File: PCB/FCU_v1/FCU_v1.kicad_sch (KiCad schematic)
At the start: 20 parts, among them J1 Conn_01x04_Pin, J10 Conn_01x04_Pin, J5 Conn_01x04_Pin, J6 Conn_01x04_Pin, J7 Conn_01x04_Pin, J8 Conn_01x04_Pin, J9 Conn_01x04_Pin, U1 TPS62132

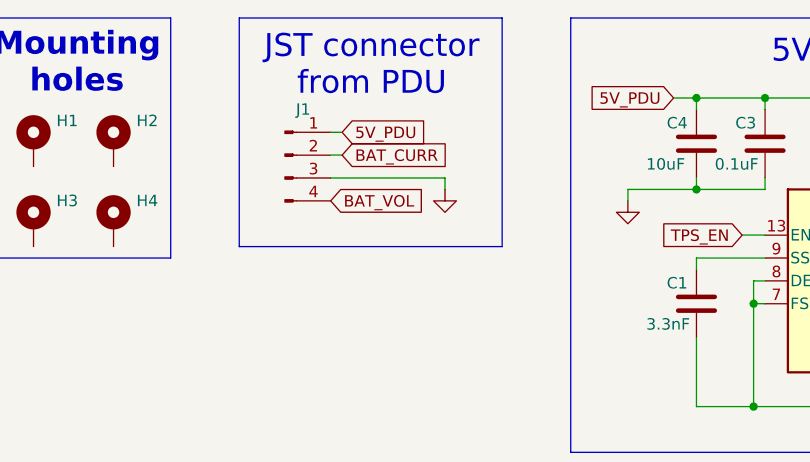
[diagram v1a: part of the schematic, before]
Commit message: Update PCB footprints, positions and backups
Remove old FCU_v1 backup zips and add new timestamped backups. Apply extensive edits to PCB/FCU_v1.kicad_pcb: reposition and rotate multiple footprints, fix pad orientations, update silkscreen/fab/crtyd outlines and UUIDs, change some net mappings and sheet/path references, and replace a resistor footprint with a SOT-23-6 ESD device (USBLC6) including updated properties and datasheet. Update related project/schematic files (FCU_v1.kicad_prl, FCU_v1.kicad_sch, PERIPHERALS.kicad_sch) to reflect these changes.
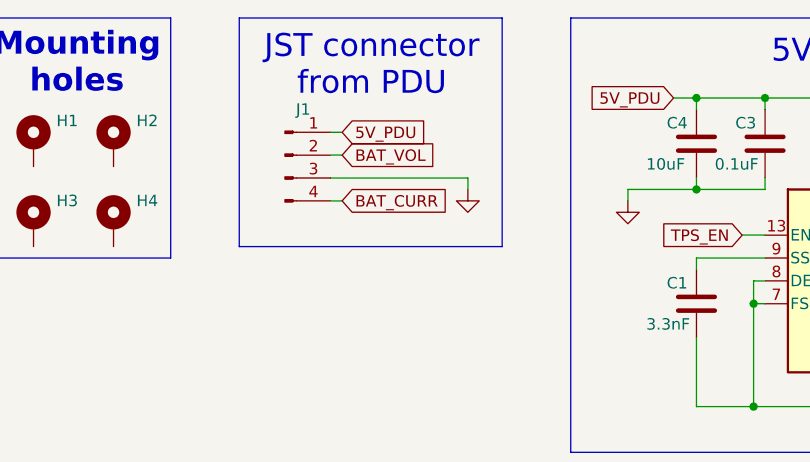
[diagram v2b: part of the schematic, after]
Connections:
- net BAT_CURR: now also J1.4 (Pin_4); no longer J1.2 (Pin_2)
- net BAT_VOL: now also J1.2 (Pin_2); no longer J1.4 (Pin_4)
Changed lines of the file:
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@@
 	(wire
 		(pts
-			(xy 69.85 36.83) (xy 69.85 38.1)
+			(xy 72.39 36.83) (xy 72.39 38.1)
 		)
 		(stroke
@@
 	(wire
 		(pts
+			(xy 57.15 39.37) (xy 58.42 39.37)
+		)
+		(stroke
+			(width 0)
+			(type default)
+		)
+	)
+	(wire
+		(pts
 			(xy 104.14 48.26) (xy 104.14 50.8)
 		)
@@
 	(wire
 		(pts
-			(xy 57.15 36.83) (xy 69.85 36.83)
+			(xy 57.15 36.83) (xy 72.39 36.83)
 		)
 		(stroke
@@
 		)
 	)
-	(global_label "BAT_CURR"
-		(shape input)
-		(at 58.42 34.29 0)
-		(fields_autoplaced yes)
-		(effects
-			(font
-				(size 1.27 1.27)
-			)
-			(justify left)
-		)
-		(property "Intersheetrefs" "${INTERSHEET_REFS}"
-			(at 70.8395 34.29 0)
-			(effects
-				(font
-					(size 1.27 1.27)
-				)
-				(justify left)
-				(hide yes)
-			)
-		)
-	)
 	(global_label "3V3"
 		(shape input)
@@
 		)
 	)
-	(global_label "3V3"
+	(global_label "BAT_VOL"
 		(shape input)
-		(at 33.02 87.63 0)
+		(at 58.42 34.29 0)
 		(fields_autoplaced yes)
 		(effects
@@
 		)
 		(property "Intersheetrefs" "${INTERSHEET_REFS}"
-			(at 39.5128 87.63 0)
+			(at 69.1462 34.29 0)
 			(effects
 				(font
@@
 		)
 	)
-	(global_label "CAN_H"
+	(global_label "3V3"
 		(shape input)
-		(at 33.02 111.76 0)
+		(at 33.02 87.63 0)
 		(fields_autoplaced yes)
 		(effects
@@
 		)
 		(property "Intersheetrefs" "${INTERSHEET_REFS}"
-			(at 41.9924 111.76 0)
+			(at 39.5128 87.63 0)
 			(effects
 				(font
@@
 		)
 	)
-	(global_label "3V3"
+	(global_label "CAN_H"
 		(shape input)
-		(at 33.02 104.14 0)
+		(at 33.02 111.76 0)
 		(fields_autoplaced yes)
 		(effects
@@
 		)
 		(property "Intersheetrefs" "${INTERSHEET_REFS}"
-			(at 39.5128 104.14 0)
+			(at 41.9924 111.76 0)
 			(effects
 				(font
@@
 		)
 	)
-	(global_label "BAT_VOL"
+	(global_label "3V3"
 		(shape input)
-		(at 57.15 39.37 0)
+		(at 33.02 104.14 0)
 		(fields_autoplaced yes)
 		(effects
@@
 		)
 		(property "Intersheetrefs" "${INTERSHEET_REFS}"
-			(at 67.8762 39.37 0)
+			(at 39.5128 104.14 0)
 			(effects
 				(font
@@
 		)
 	)
+	(global_label "BAT_CURR"
+		(shape input)
+		(at 58.42 39.37 0)
+		(fields_autoplaced yes)
+		(effects
+			(font
+				(size 1.27 1.27)
+			)
+			(justify left)
+		)
+		(property "Intersheetrefs" "${INTERSHEET_REFS}"
+			(at 70.8395 39.37 0)
+			(effects
+				(font
+					(size 1.27 1.27)
+				)
+				(justify left)
+				(hide yes)
+			)
+		)
+	)
 	(global_label "CAN_L"
 		(shape input)
@@
 	(symbol
 		(lib_id "power:GND")
-		(at 69.85 38.1 0)
+		(at 72.39 38.1 0)
 		(unit 1)
 		(exclude_from_sim no)
@@
 		(fields_autoplaced yes)
 		(property "Reference" "#PWR016"
-			(at 69.85 44.45 0)
+			(at 72.39 44.45 0)
 			(effects
 				(font
@@
 		)
 		(property "Value" "GND"
-			(at 69.85 43.18 0)
+			(at 72.39 43.18 0)
 			(effects
 				(font
@@
 		)
 		(property "Footprint" ""
-			(at 69.85 38.1 0)
+			(at 72.39 38.1 0)
 			(effects
 				(font
@@
 		)
 		(property "Datasheet" ""
-			(at 69.85 38.1 0)
+			(at 72.39 38.1 0)
 			(effects
 				(font
@@
 		)
 		(property "Description" "Power symbol creates a global label with name \"GND\" , ground"
-			(at 69.85 38.1 0)
+			(at 72.39 38.1 0)
 			(effects
 				(font

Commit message: Schematic update
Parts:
- removed C3: 0.1uF, Capacitor_SMD:C_0805_2012Metric, symbol Device:C
- removed L2: 2.2uH, Inductor_SMD:L_Coilcraft_XxL4020, symbol Device:L
- removed U1: TPS62132, Package_DFN_QFN:VQFN-16-1EP_3x3mm_P0.5mm_EP1.68x1.68mm_ThermalVias, symbol Regulator_Switching:TPS62132
- added C17: 22u, Capacitor_SMD:C_0805_2012Metric, symbol Device:C
- added C20: 100n, Capacitor_SMD:C_0805_2012Metric, symbol Device:C
- added D3: BAT54CWFILMY, Package_TO_SOT_SMD:SOT-323_SC-70, symbol Diode:BAT54CW
- added D6: SMF54A, Diode_SMD:D_SMF, symbol Diode:SMF54A
- added FB2: 120R at 100 MHz, Inductor_SMD:L_0805_2012Metric, symbol Device:FerriteBead
- added J11: USB_C_Receptacle_USB2.0_16P, Connector_USB:USB_C_Receptacle_GCT_USB4105-xx-A_16P_TopMnt_Horizontal, symbol Connector:USB_C_Receptacle_USB2.0_16P
- added L1: 744042001, SamacSys_Parts:WE-TPC_4818_482892, symbol SamacSys_Parts:744042001
- added R35, R36: 5k1, Resistor_SMD:R_0603_1608Metric, symbol Device:R
- added R37: 100k, Resistor_SMD:R_0603_1608Metric, symbol Device:R
- added R4: 33k, Resistor_SMD:R_0603_1608Metric, symbol Device:R
- added R5: 82k, Resistor_SMD:R_0603_1608Metric, symbol Device:R
- added U1: TPS62A02APDDCR, Package_TO_SOT_SMD:SOT-23-6, symbol Regulator_Switching:TPS62A02APDDC
- added U8: USBLC6-2SC6, Package_TO_SOT_SMD:SOT-23-6, symbol Power_Protection:USBLC6-2SC6
- C1: value 3.3nF -> 22u/10V
- C2: value 22uF -> 100n/10V
- C4: value 10uF -> 10u/10V
- R1: value 100k -> 2k
- R2: value 4.7k -> 450k
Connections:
- net GND: now also C17.2, C20.2, D6.2 (A2), J11.A1 (GND), J11.A12 (GND), J11.B1 (GND), J11.B12 (GND), J11.S1 (SHIELD), R35.1, R36.1, R37.2, R5.1, U1.2 (GND), U1.5 (PG), U8.2 (GND)
- net at D1.2 (A): now also R1.2; no longer R2.2
- net +3.3V: now reaches C1.1
- net +3.3V: now also R1.1, R2.1, L1.2
- net 3V3 renamed +5V
- net +5V: now also J1.1 (Pin_1), D3.2; no longer C2.1, R1.1, R2.1
- net 5V_PDU renamed +5V_FCU
- net +5V_FCU: now also C2.1, D3.3, U1.1 (EN), U1.4 (VIN); no longer J1.1 (Pin_1)
- new net: J11.A5 (CC1), R36.2
- new net: L1.1, U1.3 (SW)
- new net: R2.2, R37.1, U1.6 (FB)
- new net: J11.B5 (CC2), R35.2
- new net +VBUS: C17.1, C20.1, D3.1, FB2.2, R4.2
- new net D+: J11.A6 (D+), J11.B6 (D+), U8.6 (I/O1)
- new net D-: J11.A7 (D-), J11.B7 (D-), U8.4 (I/O2)
- new net USB_D+: U8.1 (I/O1)
- new net USB_D-: U8.3 (I/O2)
- new net USB_VBUS: D6.1 (A1), FB2.1, J11.A4 (VBUS), J11.A9 (VBUS), J11.B4 (VBUS), J11.B9 (VBUS), U8.5 (VBUS)
- new net VBUS_SENS: R4.1, R5.2
- no-connect marks 0 -> 2
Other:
- sheet PERIPHERALS renamed OLD_UNUSED
- added sheet ESP (ESP.kicad_sch)
- added sheet IMU (IMU.kicad_sch)
- sheet OLD_UNUSED: file PERIPHERALS.kicad_sch -> OLD_UNUSED.kicad_sch
- note added: "BAT54CWFILMY"
- note added: "PDB/USB 5V source"
- note added: "To STM for measurements"
- note added: "USB"
- note added: "Wurth 744042001"
- moved on the sheet: C4, D1, H1, H2, H3, H4, J1, J10, J5, J6, J7, J8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

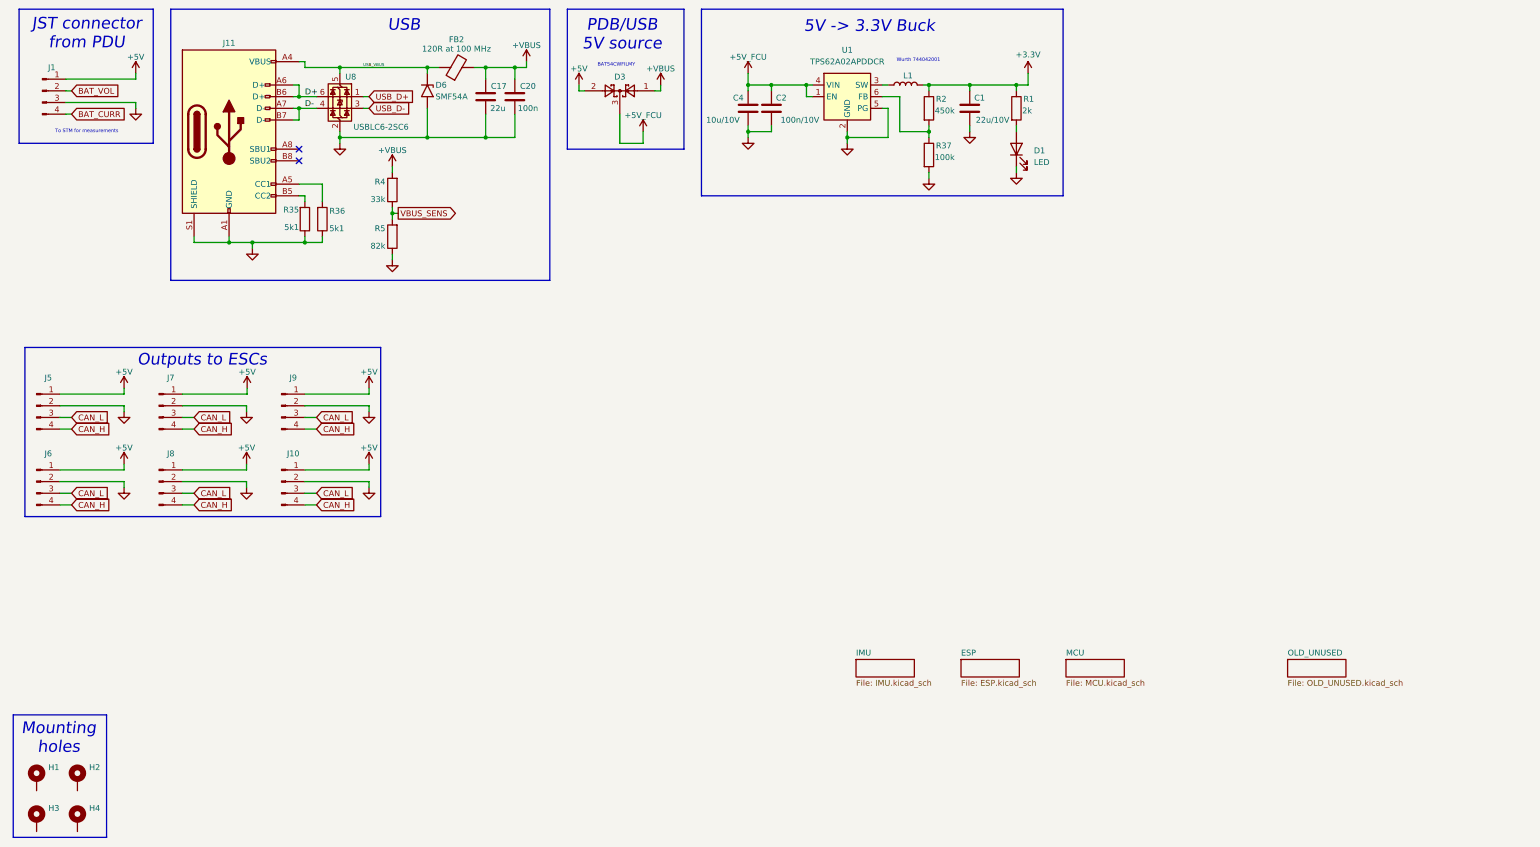
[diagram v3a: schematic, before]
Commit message: Components change and layout update
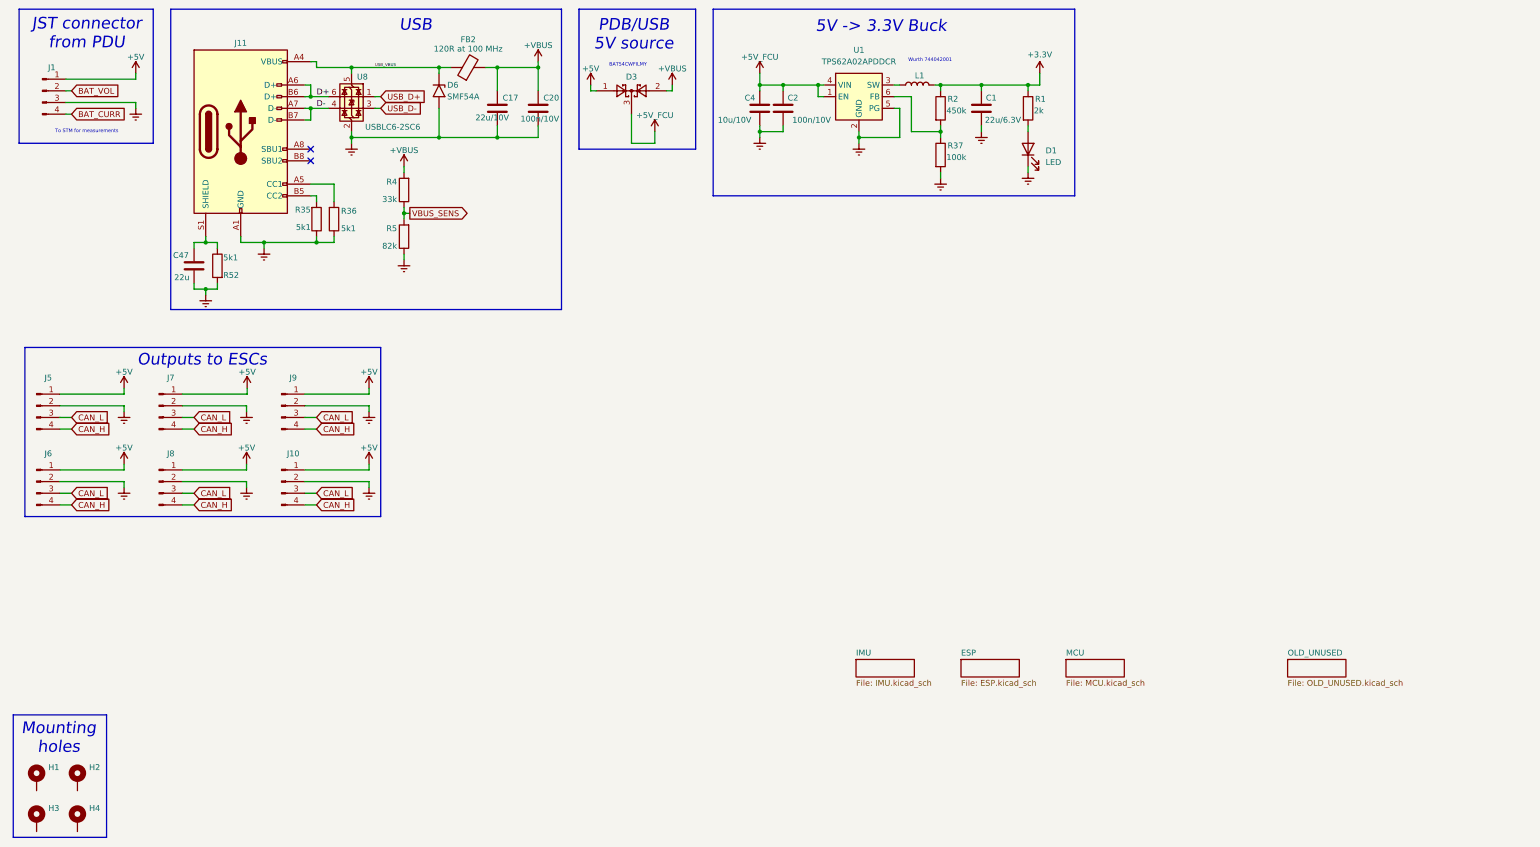
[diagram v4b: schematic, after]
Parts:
- added C47: 22u, Capacitor_SMD:C_0805_2012Metric, symbol Device:C
- added R52: 5k1, Resistor_SMD:R_0603_1608Metric, symbol Device:R
- C1: value 22u/10V -> 22u/6.3V
- C17: value 22u -> 22u/10V
- C2: footprint Capacitor_SMD:C_0805_2012Metric -> Capacitor_SMD:C_0603_1608Metric
- C20: value 100n -> 100n/10V
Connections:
- net +5V: now also D3.1; no longer D3.2
- net +VBUS: now also D3.2; no longer D3.1
- net GND: now also C47.2, R52.2; no longer J11.S1 (SHIELD)
- new net: C47.1, J11.S1 (SHIELD), R52.1
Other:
- moved on the sheet: C1, C17, C2, C20, C4, D1, D3, D6, FB2, J11, L1, R1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

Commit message: Layout update
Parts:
- removed L1: 744042001, SamacSys_Parts:WE-TPC_4818_482892, symbol SamacSys_Parts:744042001
- removed U8: USBLC6-2SC6, Package_TO_SOT_SMD:SOT-23-6, symbol Power_Protection:USBLC6-2SC6
- added L4: 744042001, SamacSys_Parts:WE-TPC_4818_482892, symbol SamacSys_Parts:744042001
- added U7: USBLC6-2SC6, Package_TO_SOT_SMD:SOT-23-6, symbol Power_Protection:USBLC6-2SC6
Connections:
- net +3.3V: now also L4.2
- net D+: now also U7.6 (I/O1)
- net D-: now also U7.4 (I/O2)
- net GND: now also U7.2 (GND)
- net USB_D+: now also U7.1 (I/O1)
- net USB_D-: now also U7.3 (I/O2)
- net USB_VBUS: now also U7.5 (VBUS)
- net SW_TPS: now reaches U1.3 (SW)
- net SW_TPS: now also L4.1
- net CAN_H renamed CAN+
- net CAN_L renamed CAN-
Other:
- moved on the sheet: R2, R37
